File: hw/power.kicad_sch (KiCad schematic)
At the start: 38 parts, among them J1501 pwr+data, U1501 TPS74612PQWDRBRQ1, U1502 LMR51430, U1503 TPS22918DBVR, U1504 TPS7A2033PDBVR, U1505 OPA320AIDBVR

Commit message: Now two CPLDs, new placement for better routing of clocks and symmetry for delay. Not routed yet but placement is "complete".
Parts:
- R1507, R1508, R1509, R1510: footprint Resistor_SMD:R_0603_1608Metric -> Resistor_SMD:R_0402_1005Metric
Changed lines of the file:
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@@
 		(on_board yes)
 		(dnp no)
-		(property "Reference" "#PWR01505"
+		(property "Reference" "#PWR01503"
 			(at 255.27 34.29 0)
 			(effects
@@
 			(project "NexRx"
 				(path "/8ae46c04-d01a-4756-8774-512b694bfaff/cbf7569b-90aa-4e1a-84a7-d4153f6242b6"
-					(reference "#PWR01505")
+					(reference "#PWR01503")
 					(unit 1)
 				)
@@
 			)
 		)
-		(property "Footprint" "Resistor_SMD:R_0603_1608Metric"
+		(property "Footprint" "Resistor_SMD:R_0402_1005Metric"
 			(at 106.426 159.004 90)
 			(effects
@@
 			)
 		)
-		(property "Footprint" "Resistor_SMD:R_0603_1608Metric"
+		(property "Footprint" "Resistor_SMD:R_0402_1005Metric"
 			(at 115.316 146.304 90)
 			(effects
@@
 		(on_board yes)
 		(dnp no)
-		(property "Reference" "#PWR01504"
+		(property "Reference" "#PWR01505"
 			(at 212.09 35.56 0)
 			(effects
@@
 			(project "NexRx"
 				(path "/8ae46c04-d01a-4756-8774-512b694bfaff/cbf7569b-90aa-4e1a-84a7-d4153f6242b6"
-					(reference "#PWR01504")
+					(reference "#PWR01505")
 					(unit 1)
 				)
@@
 			)
 		)
-		(property "Footprint" "Resistor_SMD:R_0603_1608Metric"
+		(property "Footprint" "Resistor_SMD:R_0402_1005Metric"
 			(at 87.884 159.004 90)
 			(effects
@@
 		(on_board yes)
 		(dnp no)
-		(property "Reference" "#PWR01503"
+		(property "Reference" "#PWR01504"
 			(at 201.93 35.56 0)
 			(effects
@@
 			(project "NexRx"
 				(path "/8ae46c04-d01a-4756-8774-512b694bfaff/cbf7569b-90aa-4e1a-84a7-d4153f6242b6"
-					(reference "#PWR01503")
+					(reference "#PWR01504")
 					(unit 1)
 				)
@@
 			)
 		)
-		(property "Footprint" "Resistor_SMD:R_0603_1608Metric"
+		(property "Footprint" "Resistor_SMD:R_0402_1005Metric"
 			(at 87.884 146.304 90)
 			(effects

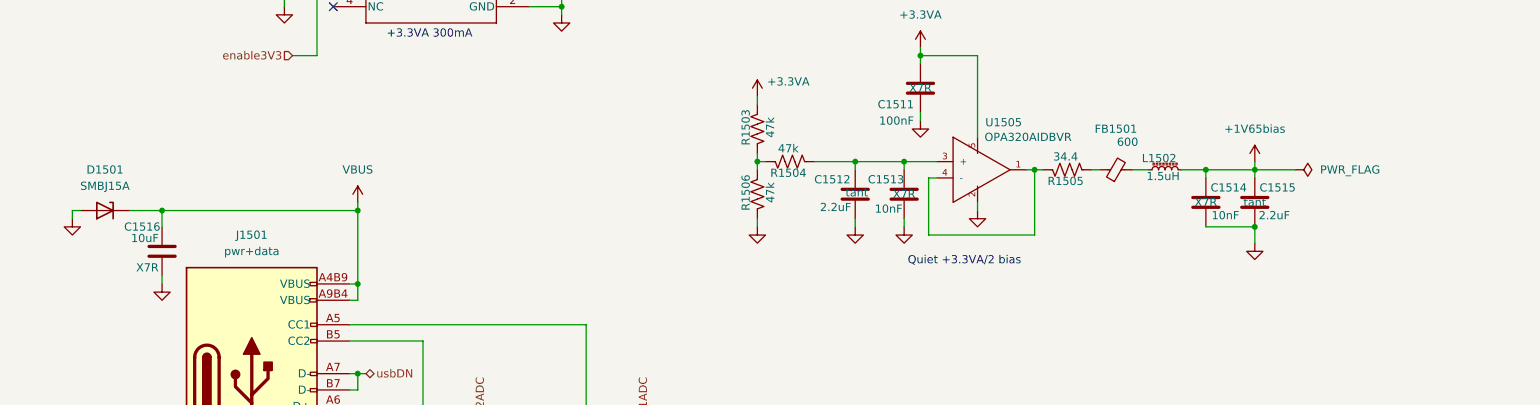
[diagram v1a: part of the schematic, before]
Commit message: Checkpoint before replicating OSD and then CPLD layout from 0 to 1
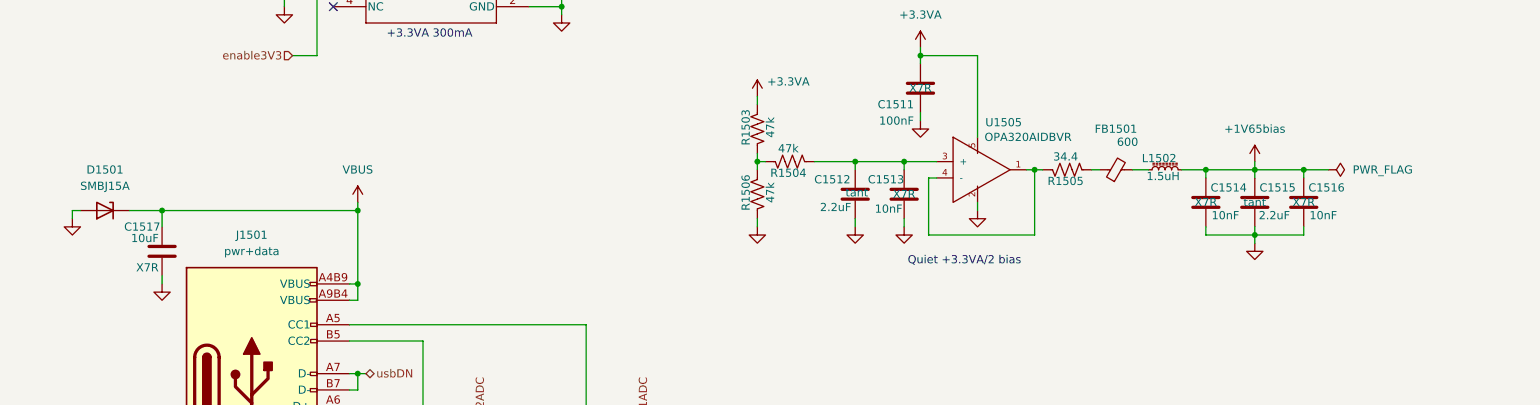
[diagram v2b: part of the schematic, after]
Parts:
- added C1516: 10nF, Capacitor_SMD:C_0603_1608Metric, symbol Device:C
- renumbered C1516 to C1517
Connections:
- net +1V65bias: now also C1516.1
- net GND: now also C1516.2

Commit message: 3D rendering now. All DRCs pass on schematic and PCB. BOM scrubbed to coallesce parts. Still no part numbers for most.
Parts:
- C1508: value 220pF -> 200pF; footprint Capacitor_SMD:C_0603_1608Metric -> Capacitor_SMD:C_0402_1005Metric; working-voltage 50V -> 25V
- C1512, C1515: footprint Capacitor_SMD:C_0805_2012Metric -> Capacitor_SMD:C_0402_1005Metric; cap-type tant -> X7R; working-voltage 10V -> 25V
- C1514, C1516: footprint Capacitor_SMD:C_0603_1608Metric -> Capacitor_SMD:C_0402_1005Metric; working-voltage 25V -> 50V
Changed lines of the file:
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@@
 			)
 		)
-		(property "Value" "220pF"
+		(property "Value" "200pF"
 			(at 187.706 45.72 0)
 			(effects
@@
 			)
 		)
-		(property "Footprint" "Capacitor_SMD:C_0603_1608Metric"
+		(property "Footprint" "Capacitor_SMD:C_0402_1005Metric"
 			(at 183.1848 39.37 0)
 			(effects
@@
 			)
 		)
-		(property "working-voltage" "50V"
+		(property "working-voltage" "25V"
 			(at 184.15 43.18 90)
 			(effects
@@
 			)
 		)
-		(property "Footprint" "Capacitor_SMD:C_0805_2012Metric"
+		(property "Footprint" "Capacitor_SMD:C_0402_1005Metric"
 			(at 208.5848 109.22 0)
 			(effects
@@
 			)
 		)
-		(property "cap-type" "tant"
+		(property "cap-type" "X7R"
 			(at 209.55 105.41 0)
 			(effects
@@
 			)
 		)
-		(property "working-voltage" "10V"
+		(property "working-voltage" "25V"
 			(at 209.55 105.41 0)
 			(effects
@@
 			)
 		)
-		(property "Footprint" "Capacitor_SMD:C_0805_2012Metric"
+		(property "Footprint" "Capacitor_SMD:C_0402_1005Metric"
 			(at 148.2852 107.95 0)
 			(effects
@@
 			)
 		)
-		(property "cap-type" "tant"
+		(property "cap-type" "X7R"
 			(at 147.574 103.886 0)
 			(effects
@@
 			)
 		)
-		(property "working-voltage" "10V"
+		(property "working-voltage" "25V"
 			(at 147.32 104.14 0)
 			(effects
@@
 			)
 		)
-		(property "Footprint" "Capacitor_SMD:C_0603_1608Metric"
+		(property "Footprint" "Capacitor_SMD:C_0402_1005Metric"
 			(at 216.2048 109.22 0)
 			(effects
@@
 			)
 		)
-		(property "working-voltage" "25V"
+		(property "working-voltage" "50V"
 			(at 217.17 105.41 0)
 			(effects
@@
 			)
 		)
-		(property "Footprint" "Capacitor_SMD:C_0603_1608Metric"
+		(property "Footprint" "Capacitor_SMD:C_0402_1005Metric"
 			(at 200.9648 109.22 0)
 			(effects
@@
 			)
 		)
-		(property "working-voltage" "25V"
+		(property "working-voltage" "50V"
 			(at 201.93 105.41 0)
 			(effects

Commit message: Not proud of the rats nest of controls for attenuator and filter, but now I have four filters (not five), all DRC pass, 3D renders properly, and I may tidy it up a bit later.
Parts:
- C1502, C1517: cap-type X7R -> X5R
- C1504, C1509, C1510: JLCPCBpn C301928 -> (none); Manufacturer_Name Murata -> (none); Manufacturer_Part_Number GRM155R61E105KE11D -> (none); Mouser Part Number 81-GRM155R61E105KE1D -> (none)
- C1506, C1507: JLCPCBpn C327087 -> (none); Manufacturer_Name Taoup Uidem -> (none); Manufacturer_Part_Number 81-GXT155R71E223KE1D -> (none); Mouser Part Number 963-MLAST168BB5106MT -> (none); cap-type X7R -> X5R
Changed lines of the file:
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@@
 			)
 		)
-		(property "cap-type" "X7R"
+		(property "cap-type" "X5R"
 			(at 119.126 41.402 0)
 			(effects
@@
 			)
 		)
-		(property "Manufacturer_Name" "Taoup Uidem"
+		(property "Manufacturer_Name" ""
 			(at 116.84 39.37 0)
 			(effects
@@
 			)
 		)
-		(property "Manufacturer_Part_Number" "81-GXT155R71E223KE1D"
+		(property "Manufacturer_Part_Number" ""
 			(at 116.84 39.37 0)
 			(effects
@@
 			)
 		)
-		(property "Mouser Part Number" "963-MLAST168BB5106MT"
+		(property "Mouser Part Number" ""
 			(at 116.84 39.37 0)
 			(effects
@@
 			)
 		)
-		(property "JLCPCBpn" "C327087"
+		(property "JLCPCBpn" ""
 			(at 116.84 39.37 0)
 			(effects
@@
 			)
 		)
-		(property "Manufacturer_Name" "Murata"
+		(property "Manufacturer_Name" ""
 			(at 200.66 38.1 0)
 			(effects
@@
 			)
 		)
-		(property "Manufacturer_Part_Number" "GRM155R61E105KE11D"
+		(property "Manufacturer_Part_Number" ""
 			(at 200.66 38.1 0)
 			(effects
@@
 			)
 		)
-		(property "Mouser Part Number" "81-GRM155R61E105KE1D"
+		(property "Mouser Part Number" ""
 			(at 200.66 38.1 0)
 			(effects
@@
 			)
 		)
-		(property "JLCPCBpn" "C301928"
+		(property "JLCPCBpn" ""
 			(at 200.66 38.1 0)
 			(effects
@@
 			)
 		)
-		(property "cap-type" "X7R"
+		(property "cap-type" "X5R"
 			(at 48.26 40.64 0)
 			(effects
@@
 			)
 		)
-		(property "cap-type" "X7R"
+		(property "cap-type" "X5R"
 			(at 37.084 115.57 0)
 			(effects
@@
 			)
 		)
-		(property "Manufacturer_Name" "Murata"
+		(property "Manufacturer_Name" ""
 			(at 58.42 69.85 0)
 			(effects
@@
 			)
 		)
-		(property "Manufacturer_Part_Number" "GRM155R61E105KE11D"
+		(property "Manufacturer_Part_Number" ""
 			(at 58.42 69.85 0)
 			(effects
@@
 			)
 		)
-		(property "Mouser Part Number" "81-GRM155R61E105KE1D"
+		(property "Mouser Part Number" ""
 			(at 58.42 69.85 0)
 			(effects
@@
 			)
 		)
-		(property "JLCPCBpn" "C301928"
+		(property "JLCPCBpn" ""
 			(at 58.42 69.85 0)
 			(effects
@@
 			)
 		)
-		(property "cap-type" "X7R"
+		(property "cap-type" "X5R"
 			(at 129.286 41.402 0)
 			(effects
@@
 			)
 		)
-		(property "Manufacturer_Name" "Taoup Uidem"
+		(property "Manufacturer_Name" ""
 			(at 127 39.37 0)
 			(effects
@@
 			)
 		)
-		(property "Manufacturer_Part_Number" "81-GXT155R71E223KE1D"
+		(property "Manufacturer_Part_Number" ""
 			(at 127 39.37 0)
 			(effects
@@
 			)
 		)
-		(property "Mouser Part Number" "963-MLAST168BB5106MT"
+		(property "Mouser Part Number" ""
 			(at 127 39.37 0)
 			(effects
@@
 			)
 		)
-		(property "JLCPCBpn" "C327087"
+		(property "JLCPCBpn" ""
 			(at 127 39.37 0)
 			(effects
@@
 			)
 		)
-		(property "Manufacturer_Name" "Murata"
+		(property "Manufacturer_Name" ""
 			(at 101.6 69.85 0)
 			(effects
@@
 			)
 		)
-		(property "Manufacturer_Part_Number" "GRM155R61E105KE11D"
+		(property "Manufacturer_Part_Number" ""
 			(at 101.6 69.85 0)
 			(effects
@@
 			)
 		)
-		(property "Mouser Part Number" "81-GRM155R61E105KE1D"
+		(property "Mouser Part Number" ""
 			(at 101.6 69.85 0)
 			(effects
@@
 			)
 		)
-		(property "JLCPCBpn" "C301928"
+		(property "JLCPCBpn" ""
 			(at 101.6 69.85 0)
 			(effects

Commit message: Set up for DVT2 PCBA build at JLCPCB
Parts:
- C1501, C1511, C1513: MPN C0805F104K1RACAUTO -> (none)
- C1502, C1517: MPN 81-GXT155R71E223KE1D -> (none)
- C1503, C1505: MPN GRM155R61E105KE11D -> (none)
- C1508: MPN C1608C0G1H221F080AA -> (none)
- C1512, C1515: MPN TMCP1D225MTR2F -> (none)
- C1514, C1516: MPN GCM1885C2A103JE02J -> (none)
- U1503: MFG (none) -> TI; Manufacturer_Name Texas Instruments -> (none); Manufacturer_Part_Number TPS22918DBVR -> (none)
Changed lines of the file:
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@@
 			)
 		)
-		(property "MPN" "C1608C0G1H221F080AA"
+		(property "MPN" ""
 			(at 0 0 0)
 			(effects
@@
 			)
 		)
-		(property "MPN" "TMCP1D225MTR2F"
+		(property "MPN" ""
 			(at 81.28 -52.07 0)
 			(effects
@@
 			)
 		)
-		(property "MPN" "C0805F104K1RACAUTO"
+		(property "MPN" ""
 			(at 12.7 -81.28 0)
 			(effects
@@
 			)
 		)
-		(property "MPN" "GRM155R61E105KE11D"
+		(property "MPN" ""
 			(at 0 0 0)
 			(effects
@@
 			)
 		)
-		(property "MPN" "C0805F104K1RACAUTO"
+		(property "MPN" ""
 			(at 0 0 0)
 			(effects
@@
 			)
 		)
-		(property "MPN" "81-GXT155R71E223KE1D"
+		(property "MPN" ""
 			(at 0 0 0)
 			(effects
@@
 			)
 		)
-		(property "MPN" "81-GXT155R71E223KE1D"
+		(property "MPN" ""
 			(at -2.54 10.16 0)
 			(effects
@@
 			)
 		)
-		(property "MPN" "TMCP1D225MTR2F"
+		(property "MPN" ""
 			(at 208.28 -50.8 0)
 			(effects
@@
 			)
 		)
-		(property "MPN" "GCM1885C2A103JE02J"
+		(property "MPN" ""
 			(at 96.52 -52.07 0)
 			(effects
@@
 			)
 		)
-		(property "Manufacturer_Name" "Texas Instruments"
+		(property "Manufacturer_Name" ""
 			(at 191.77 729.21 0)
 			(effects
@@
 			)
 		)
-		(property "Manufacturer_Part_Number" "TPS22918DBVR"
+		(property "Manufacturer_Part_Number" ""
 			(at 191.77 829.21 0)
 			(effects
@@
 			)
 		)
+		(property "MFG" "TI"
+			(at 167.64 34.29 0)
+			(effects
+				(font
+					(size 1.27 1.27)
+				)
+				(hide yes)
+			)
+		)
 		(pin "5"
 		)
@@
 			)
 		)
-		(property "MPN" "C0805F104K1RACAUTO"
+		(property "MPN" ""
 			(at 10.16 -64.77 0)
 			(effects
@@
 			)
 		)
-		(property "MPN" "GRM155R61E105KE11D"
+		(property "MPN" ""
 			(at 0 0 0)
 			(effects
@@
 			)
 		)
-		(property "MPN" "GCM1885C2A103JE02J"
+		(property "MPN" ""
 			(at 81.28 -52.07 0)
 			(effects

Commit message: DVT2 try #2. This is the one from which I ordered PCBs (bare only) from JLCPCB
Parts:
- J1501: LCSC_PN C165948 -> C393939
- R1505: value 34.4 -> 22; JLCPCBpn (none) -> C4258780
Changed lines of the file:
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@@
 			)
 		)
-		(property "Value" "34.4"
+		(property "Value" "22"
 			(at 180.086 98.298 90)
 			(effects
@@
 			)
 		)
-		(property "Description" "Resistor, Thin Film, 0.1%, 33, 0402"
+		(property "Description" "Resistor, Thin Film, 0.1%, 22, 0402"
 			(at 180.34 100.33 0)
 			(effects
@@
 			)
 		)
+		(property "JLCPCBpn" "C4258780"
+			(at 180.34 100.33 90)
+			(effects
+				(font
+					(size 1.27 1.27)
+				)
+				(hide yes)
+			)
+		)
 		(pin "1"
 		)
@@
 			)
 		)
-		(property "LCSC_PN" "C165948"
+		(property "LCSC_PN" "C393939"
 			(at -19.05 -25.4 0)
 			(effects

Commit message: Cleaned up some vias, some traces, resubmitted to JLCPCB as DVT2-20260812.
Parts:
- removed C1508: 200pF, Capacitor_SMD:C_0402_1005Metric, symbol Device:C
- added C1508: 300pF, Capacitor_SMD:C_0402_1005Metric, symbol Device:C_US
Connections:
- net +3.3V: now also C1508.2
- net at U1503.4 (CT): now also C1508.1
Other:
- note added: "~600us 3.3V rise time"
- note removed: "~455us 3.3V rise time"
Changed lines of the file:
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@@
 		(comment 1 "Alan Mimms")
 	)
-	(text "~455us 3.3V\nrise time"
+	(text "~600us 3.3V\nrise time"
 		(exclude_from_sim no)
 		(at 184.404 51.308 0)
@@
 	)
 	(symbol
-		(lib_id "Device:C")
-		(at 184.15 43.18 180)
-		(unit 1)
-		(exclude_from_sim no)
-		(in_bom yes)
-		(on_board yes)
-		(dnp no)
-		(property "Reference" "C1508"
-			(at 187.706 40.894 0)
-			(effects
-				(font
-					(size 1.27 1.27)
-				)
-			)
-		)
-		(property "Value" "200pF"
-			(at 187.706 45.72 0)
-			(effects
-				(font
-					(size 1.27 1.27)
-				)
-			)
-		)
-		(property "Footprint" "Capacitor_SMD:C_0402_1005Metric"
-			(at 183.1848 39.37 0)
-			(effects
-				(font
-					(size 1.27 1.27)
-				)
-				(hide yes)
-			)
-		)
-		(property "Datasheet" "~"
-			(at 184.15 43.18 0)
-			(effects
-				(font
-					(size 1.27 1.27)
-				)
-				(hide yes)
-			)
-		)
-		(property "Description" "Capacitor, MLCC, NP0, 50V, 5%, 220pF, 0603"
-			(at 184.15 43.18 0)
-			(effects
-				(font
-					(size 1.27 1.27)
-				)
-				(hide yes)
-			)
-		)
-		(property "Manufacturer" "TDK"
-			(at 0 0 0)
-			(effects
-				(font
-					(size 1.27 1.27)
-				)
-				(hide yes)
-			)
-		)
-		(property "MPN" ""
-			(at 0 0 0)
-			(effects
-				(font
-					(size 1.27 1.27)
-				)
-				(hide yes)
-			)
-		)
-		(property "LCSC_PN" "C106210"
-			(at 0 0 0)
-			(effects
-				(font
-					(size 1.27 1.27)
-				)
-				(hide yes)
-			)
-		)
-		(property "Mouser_PN" "810-C1608C0G1H221F"
-			(at 0 0 0)
-			(effects
-				(font
-					(size 1.27 1.27)
-				)
-				(hide yes)
-			)
-		)
-		(property "cap-type" "NP0"
-			(at 184.15 43.18 0)
-			(effects
-				(font
-					(size 1.27 1.27)
-				)
-			)
-		)
-		(property "working-voltage" "25V"
-			(at 184.15 43.18 90)
-			(effects
-				(font
-					(size 1.27 1.27)
-				)
-				(hide yes)
-			)
-		)
-		(property "Core" ""
-			(at 184.15 43.18 90)
-			(effects
-				(font
-					(size 1.27 1.27)
-				)
-				(hide yes)
-			)
-		)
-		(property "label" ""
-			(at 184.15 43.18 90)
-			(effects
-				(font
-					(size 1.27 1.27)
-				)
-				(hide yes)
-			)
-		)
-		(property "Winding" ""
-			(at 184.15 43.18 0)
-			(effects
-				(font
-					(size 1.27 1.27)
-				)
-				(hide yes)
-			)
-		)
-		(pin "2"
-		)
-		(pin "1"
-		)
-		(instances
-			(project "NexRx"
-				(path "/8ae46c04-d01a-4756-8774-512b694bfaff/cbf7569b-90aa-4e1a-84a7-d4153f6242b6"
-					(reference "C1508")
-					(unit 1)
-				)
-			)
-		)
-	)
-	(symbol
 		(lib_id "Library:OPA320AIDBVR")
 		(at 165.1 100.33 0)
@@
 					(unit 1)
 				)
+			)
+		)
+	)
+	(symbol
+		(lib_id "Device:C_US")
+		(at 184.15 43.18 0)
+		(unit 1)
+		(exclude_from_sim no)
+		(in_bom yes)
+		(on_board yes)
+		(dnp no)
+		(property "Reference" "C1508"
+			(at 187.452 40.894 0)
+			(effects
+				(font
+					(size 1.27 1.27)
+				)
+			)
+		)
+		(property "Value" "300pF"
+			(at 187.706 45.974 0)
+			(effects
+				(font
+					(size 1.27 1.27)
+				)
+			)
+		)
+		(property "Footprint" "Capacitor_SMD:C_0402_1005Metric"
+			(at 184.15 43.18 0)
+			(effects
+				(font
+					(size 1.27 1.27)
+				)
+				(hide yes)
+			)
+		)
+		(property "Datasheet" ""
+			(at 184.15 43.18 0)
+			(effects
+				(font
+					(size 1.27 1.27)
+				)
+				(hide yes)
+			)
+		)
+		(property "Description" "capacitor, US symbol"
+			(at 184.15 43.18 0)
+			(effects
+				(font
+					(size 1.27 1.27)
+				)
+				(hide yes)
+			)
+		)
+		(property "Winding" ""
+			(at 184.15 43.18 90)
+			(effects
+				(font
+					(size 1.27 1.27)
+				)
+				(hide yes)
+			)
+		)
+		(property "cap-type" "NP0"
+			(at 184.15 43.18 0)
+			(effects
+				(font
+					(size 1.27 1.27)
+				)
+			)
+		)
+		(property "r-power" ""
+			(at 184.15 43.18 0)
+			(effects
+				(font
+					(size 1.27 1.27)
+				)
+			)
+		)
+		(property "label" ""
+			(at 184.15 43.18 0)
+			(effects
+				(font
+					(size 1.27 1.27)
+				)
+			)
+		)
+		(property "Mouser Part Number" ""
+			(at 184.15 43.18 90)
+			(effects
+				(font
+					(size 1.27 1.27)
+				)
+				(hide yes)
+			)
+		)
+		(property "MPN" ""
+			(at 184.15 43.18 90)
+			(effects
+				(font
+					(size 1.27 1.27)
+				)
+				(hide yes)
+			)
+		)
+		(property "Manufacturer" "KEMET"
+			(at 184.15 43.18 90)
+			(effects
+				(font
+					(size 1.27 1.27)
+				)
+				(hide yes)
+			)
+		)
+		(property "Mouser_PN" "80-C0402C132J5GACTU"
+			(at 184.15 43.18 90)
+			(effects
+				(font
+					(size 1.27 1.27)
+				)
+				(hide yes)
+			)
+		)
+		(property "working-voltage" "25V"
+			(at 184.15 43.18 90)
+			(effects
+				(font
+					(size 1.27 1.27)
+				)
+				(hide yes)
+			)
+		)
+		(pin "1"
+		)
+		(pin "2"
+		)
+		(instances
+			(project "NexRx"
+				(path "/8ae46c04-d01a-4756-8774-512b694bfaff/cbf7569b-90aa-4e1a-84a7-d4153f6242b6"
+					(reference "C1508")
+					(unit 1)
+				)
